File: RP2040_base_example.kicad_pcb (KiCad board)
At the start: 2 copper layers, 24 parts, among them SW1 SW_Push, U1 W25Q16JV, U2 RP2040, Y2 ECS-120-8-33-JGN-TR3

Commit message: Reannotate
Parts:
- added C17: 10u, Capacitor_SMD:C_0603_1608Metric, F.Cu at (103.2, 60.7)
- added C18: 22u, Capacitor_SMD:C_0603_1608Metric, F.Cu at (103.2, 63.2)
- added J1: Conn_01x17, Connector_PinHeader_1.27mm:PinHeader_1x17_P1.27mm_Vertical, F.Cu at (95.0, 52.9)
- added J2: Conn_01x17, Connector_PinHeader_1.27mm:PinHeader_1x17_P1.27mm_Vertical, F.Cu at (99.2, 52.9)
- added R5: 4.7, Resistor_SMD:R_0603_1608Metric, F.Cu at (103.2, 65.7)
- added SWD1: Conn_01x03, Connector_PinHeader_1.27mm:PinHeader_1x03_P1.27mm_Vertical, F.Cu at (107.3, 61.1)
- added U3: AMS1117-3.3, Package_TO_SOT_SMD:SOT-223-3_TabPin2, F.Cu at (106.2, 55.3)
- renumbered C18 to C1, C9 to C10, C6 to C11, C7 to C12, C31 to C13, C32 to C14, C29 to C15, C30 to C16, C19 to C2, C8 to C3, C5 to C4, C4 to C5, C3 to C6, C2 to C7, C1 to C8, C28 to C9, R6 to R1, R7 to R2, R10 to R3, R8 to R4, U2 to U1, U1 to U2, Y2 to Y1
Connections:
- net /RP2040-base/GND renamed GND
- net /RP2040-base/VIN renamed +3V3
- U1 pad 38: /RP2040-base/GPIO26_ADC0 -> /RP2040-base/GPIO26
- U1 pad 39: /RP2040-base/GPIO27_ADC1 -> /RP2040-base/GPIO27
- U1 pad 40: /RP2040-base/GPIO28_ADC2 -> /RP2040-base/GPIO28
- U1 pad 41: /RP2040-base/GPIO19_ADC3 -> /RP2040-base/GPIO29

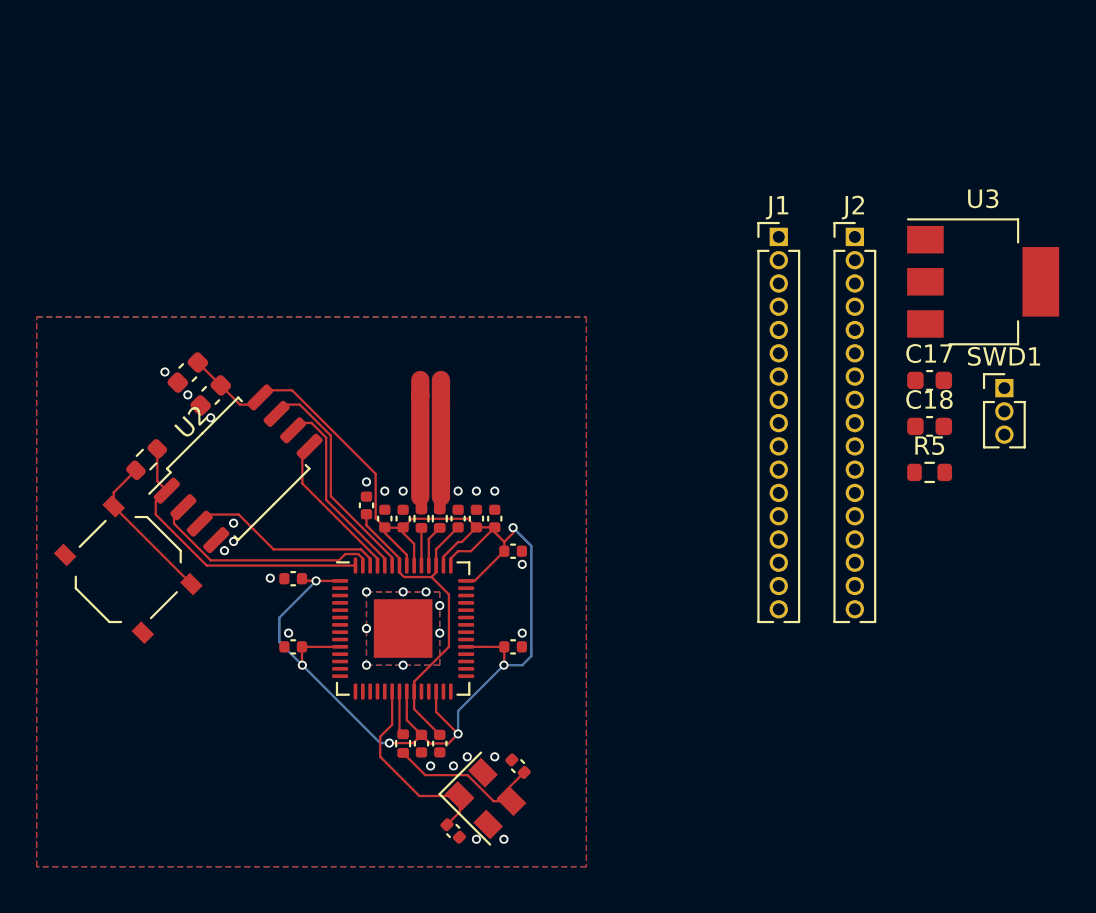
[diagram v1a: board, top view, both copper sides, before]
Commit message: Complete pcb + jlcpcb production files for part placement test on website
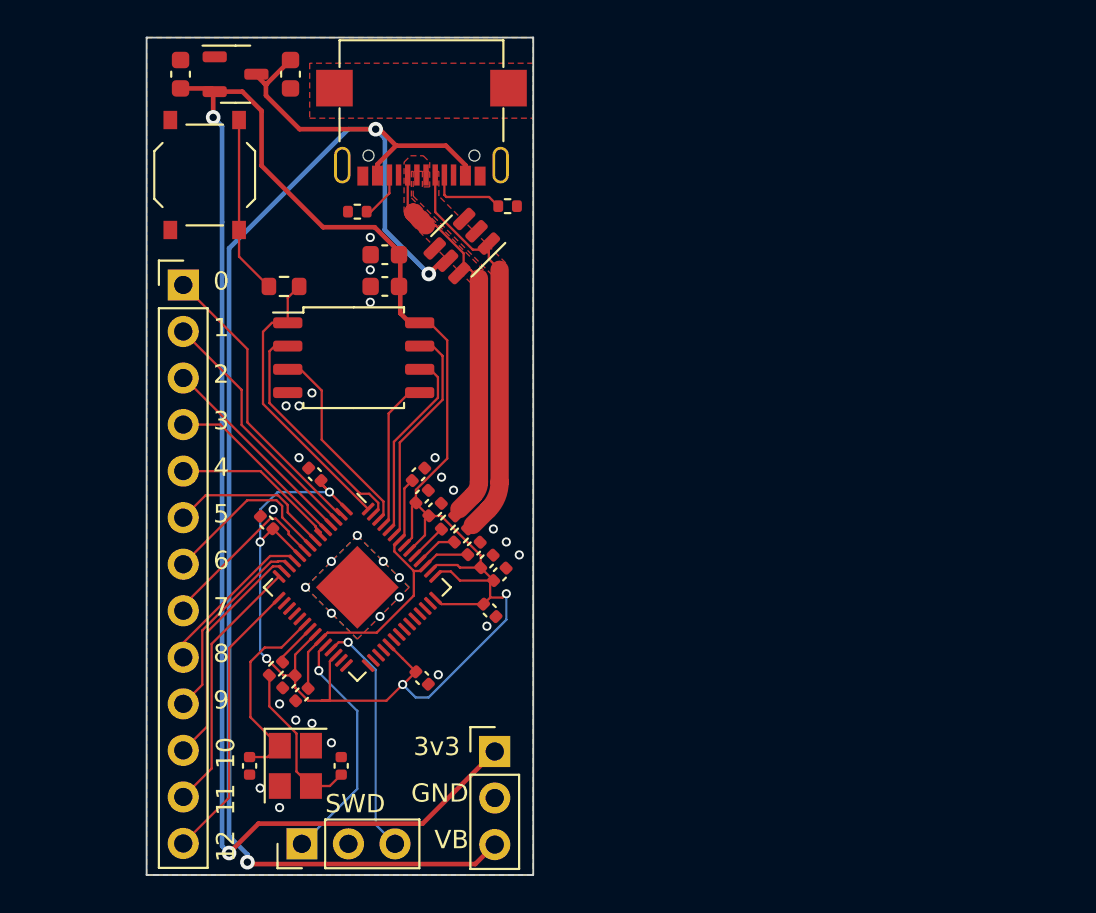
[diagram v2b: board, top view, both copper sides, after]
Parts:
- removed the C17 at (103.2, 60.7)
- removed the R5 at (103.2, 65.7)
- removed the U3 at (106.2, 55.3)
- added C1: 1u, Capacitor_SMD:C_0603_1608Metric, F.Cu at (68.4, 44.0)
- added J3: GT-USB-7047C, footprints:GT-USB-7047C, F.Cu at (75.5, 47.0)
- added R1: 5k1, Resistor_SMD:R_0402_1005Metric, F.Cu at (80.2, 51.2)
- added R2: 5k1, Resistor_SMD:R_0402_1005Metric, F.Cu at (72.0, 51.5)
- added U1: XC6206P332MR, Package_TO_SOT_SMD:SOT-23-3, F.Cu at (65.4, 44.0)
- added U2: SRV05-4, Package_TO_SOT_SMD:SOT-23-6, F.Cu at (77.7, 53.4)
- C2: renamed from C18; value 22u -> 1u
- J1: value Conn_01x17 -> Conn_01x03; footprint Connector_PinHeader_1.27mm:PinHeader_1x17_P1.27mm_Vertical -> Connector_PinHeader_2.54mm:PinHeader_1x03_P2.54mm_Vertical
- J2: value Conn_01x17 -> Conn_01x13; footprint Connector_PinHeader_1.27mm:PinHeader_1x17_P1.27mm_Vertical -> Connector_PinHeader_2.54mm:PinHeader_1x13_P2.54mm_Vertical
- SWD1: footprint Connector_PinHeader_1.27mm:PinHeader_1x03_P1.27mm_Vertical -> Connector_PinHeader_2.54mm:PinHeader_1x03_P2.54mm_Vertical
- U4: renamed from U2; value W25Q16JV -> W25QXXXJV
- Y1: value ECS-120-8-33-JGN-TR3 -> X322512MSB4SI; footprint Crystal:Crystal_SMD_EuroQuartz_MT-4Pin_3.2x2.5mm -> RP2040_base:YSX321SL, datasheet recommended measurements
- moved SWD1 45.7 mm to (69.0, 86.0), turned to 90 degrees
- moved C2 45.2 mm to (62.4, 44.0), turned to 90 degrees
- moved J2 36.7 mm to (62.5, 55.5)
- moved J1 32.1 mm to (79.5, 81.0)
- moved SW1 21.9 mm to (63.7, 49.5), turned to 90 degrees
- moved C17 12.5 mm to (73.5, 53.9), turned to 180 degrees
- moved R6 12.1 mm to (68.0, 55.6), turned to 180 degrees
- moved C15 11.7 mm to (66.1, 81.7), turned to -90 degrees
- moved C18 11.2 mm to (73.5, 55.6), turned to 180 degrees
- moved Y1 10.5 mm to (68.6, 81.7), turned to -90 degrees
- moved C16 9.65 mm to (71.1, 81.7), turned to 90 degrees
- moved U4 8.74 mm to (71.8, 59.5), turned to 0 degrees
- moved R5 8.06 mm to (67.6, 76.4), turned to -135 degrees
- moved C3 7.99 mm to (69.0, 77.9), turned to -135 degrees
- moved C8 7.99 mm to (68.3, 77.1), turned to -135 degrees
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- renumbered C8 to C10, C9 to C11, C10 to C12, C11 to C13, C12 to C14, C13 to C15, C14 to C16, C15 to C17, C16 to C18, C1 to C3, C2 to C4, C3 to C5, C4 to C6, C5 to C7, C6 to C8, C7 to C9, R1 to R3, R2 to R4, R3 to R5, R4 to R6, U1 to U3
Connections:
- C2 pad 1: Net-(C18-Pad1) -> +3V3
- J1 pad 1: VBUS -> +3V3
- J1 pad 3: /RP2040-base/GPIO0 -> VBUS
- J2 pad 1: /RP2040-base/GPIO29 -> /RP2040-base/GPIO0
- J2 pad 10: /RP2040-base/GPIO20 -> /RP2040-base/GPIO9
- J2 pad 11: /RP2040-base/GPIO19 -> /RP2040-base/GPIO10
- J2 pad 12: /RP2040-base/GPIO18 -> /RP2040-base/GPIO11
- J2 pad 13: /RP2040-base/GPIO17 -> /RP2040-base/GPIO12
- J2 pad 2: /RP2040-base/GPIO28 -> /RP2040-base/GPIO1
- J2 pad 3: /RP2040-base/GPIO27 -> /RP2040-base/GPIO2
- J2 pad 4: /RP2040-base/GPIO26 -> /RP2040-base/GPIO3
- J2 pad 5: /RP2040-base/GPIO25 -> /RP2040-base/GPIO4
- J2 pad 6: /RP2040-base/GPIO24 -> /RP2040-base/GPIO5
- J2 pad 7: /RP2040-base/GPIO23 -> /RP2040-base/GPIO6
- J2 pad 8: /RP2040-base/GPIO22 -> /RP2040-base/GPIO7
- J2 pad 9: /RP2040-base/GPIO21 -> /RP2040-base/GPIO8
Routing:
- net VBUS: track 0.00 -> 87.3 mm, vias 0 -> 3
- net +3V3: track 84.2 -> 160.7 mm, vias 6 -> 7
- net /RP2040-base/GPIO0: track 0.00 -> 16.2 mm
- net /RP2040-base/GPIO12: track 0.00 -> 15.6 mm
- net /RP2040-base/USB_D-: track 7.08 -> 22.1 mm
- net /RP2040-base/GPIO11: track 0.00 -> 14.2 mm
- net /RP2040-base/USB_D+: track 7.08 -> 21.2 mm
- net /RP2040-base/GPIO1: track 0.00 -> 13.7 mm
- net /RP2040-base/SWD: track 0.00 -> 13.2 mm, vias 0 -> 1
- net /RP2040-base/SWCLK: track 0.00 -> 13.2 mm, vias 0 -> 1
- net /RP2040-base/GPIO10: track 0.00 -> 12.8 mm
- net /RP2040-base/GPIO2: track 0.00 -> 11.4 mm
- net /RP2040-base/GPIO9: track 0.00 -> 10.9 mm
- net /RP2040-base/GPIO3: track 0.00 -> 10.2 mm
- net /RP2040-base/GPIO6: track 0.00 -> 9.76 mm
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- added copper zone on F.Cu, net /RP2040-base/USB_D+
- added copper zone on F.Cu, net /RP2040-base/USB_D-
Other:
- board outline added: 21.1 x 45.7 mm
- board text added: "0"
- board text added: "1"
- board text added: "10"
- board text added: "11"
- board text added: "12"
- board text added: "2"
- board text added: "3"
- board text added: "3v3"
- board text added: "4"
- board text added: "5"
- board text added: "6"
- board text added: "7"
- board text added: "8"
- board text added: "9"
- board text added: "GND"
- board text added: "SWD"
- board text added: "VB"

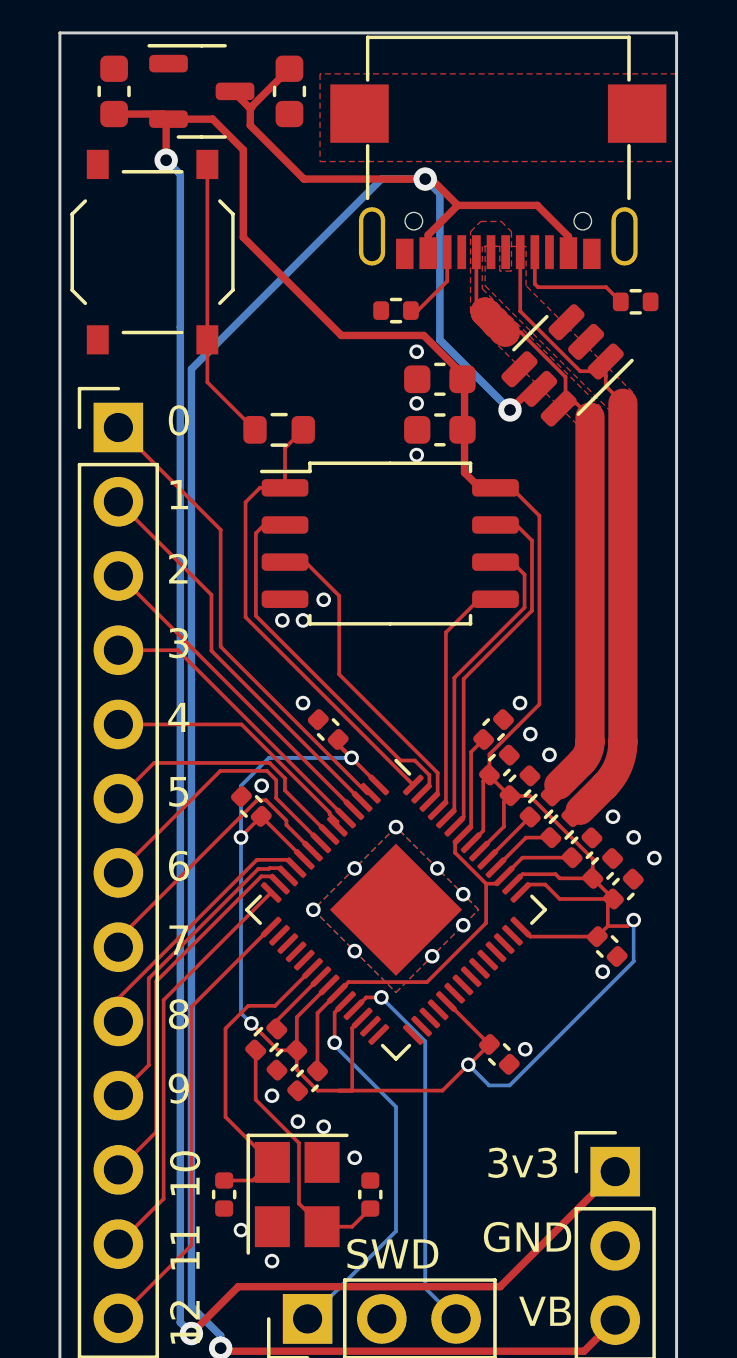
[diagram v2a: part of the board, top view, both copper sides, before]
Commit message: Rotate footprints to coincide with jlcpcb rotation
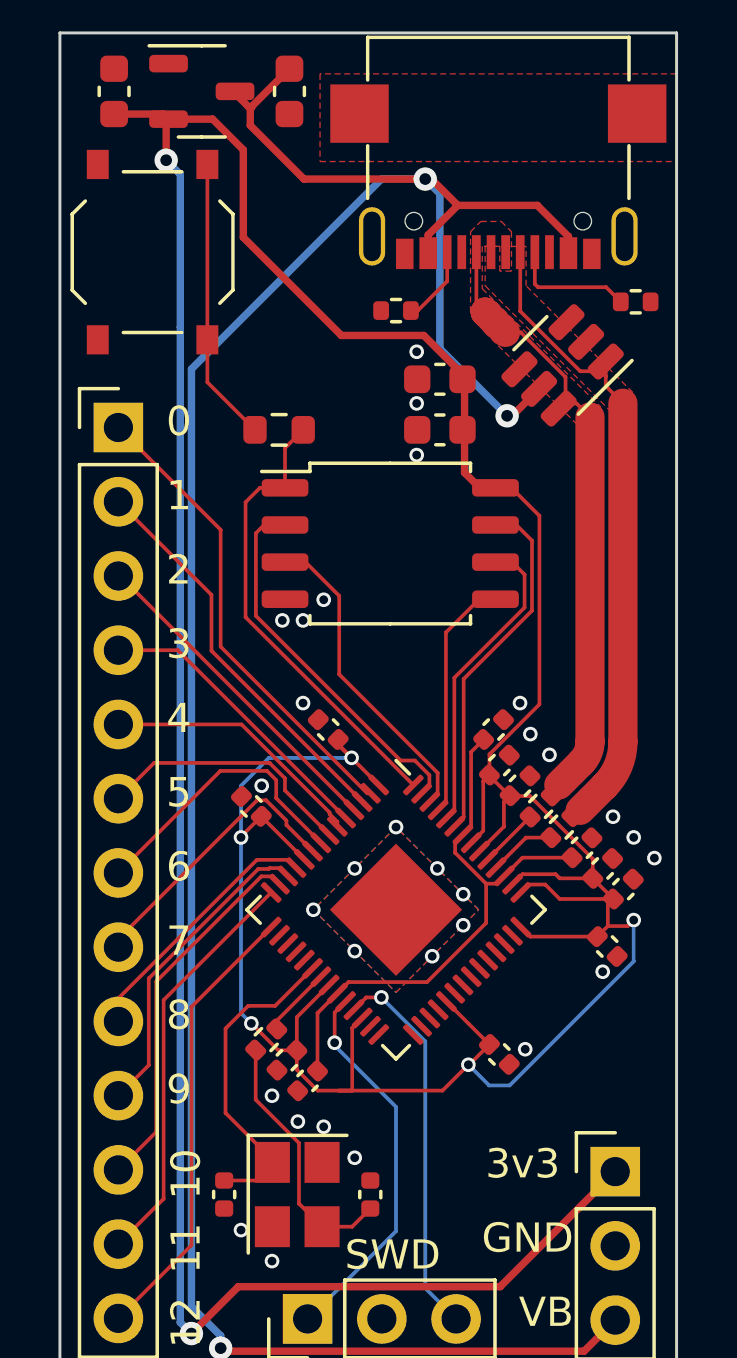
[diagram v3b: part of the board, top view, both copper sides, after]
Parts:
- U1: footprint Package_TO_SOT_SMD:SOT-23-3 -> footprints:SOT-23-3_flipped_for_jlcpcb
- U2: footprint Package_TO_SOT_SMD:SOT-23-6 -> footprints:SOT-23-6_flipped_for_jlcpcb
- Ur: renamed from U4; footprint Package_SO:SOIC-8_5.275x5.275mm_P1.27mm -> RP2040_base:SOIC-8_5.275x5.275mm_P1.27mm
- turned U1 to 180 degrees
- turned U2 to 45 degrees
- turned Ur to -90 degrees
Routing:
- net /RP2040-base/XIN: track 10.9 -> 11.7 mm

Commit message: Add title blocks, and set version to 0.9 (will bump to 1.0 if ordered and tested)
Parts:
- renumbered Ur to U4
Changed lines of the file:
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@@
   )
   (paper "A4")
+  (title_block
+    (title "RP2040-base example")
+    (date "2023-07-30")
+    (rev "0.9")
+    (company "https://github.com/TT-392/RP2040-base-example")
+  )
   (layers
     (0 "F.Cu" signal)
@@
     (property "ki_keywords" "flash memory SPI")
     (attr smd)
-    (fp_text reference "Ur" (at 3.59 0) (layer "F.SilkS") hide
-        (effects (font (size 1 1) (thickness 0.15)))
-    )
+    (fp_text reference "U4" (at 3.59 0) (layer "F.SilkS") hide
+        (effects (font (size 1 1) (thickness 0.15)))
+    )
